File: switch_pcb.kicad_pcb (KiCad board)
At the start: 2 copper layers, 50 x 34 mm, 8 parts, among them J1 3x5mm, SW1 Microswitch

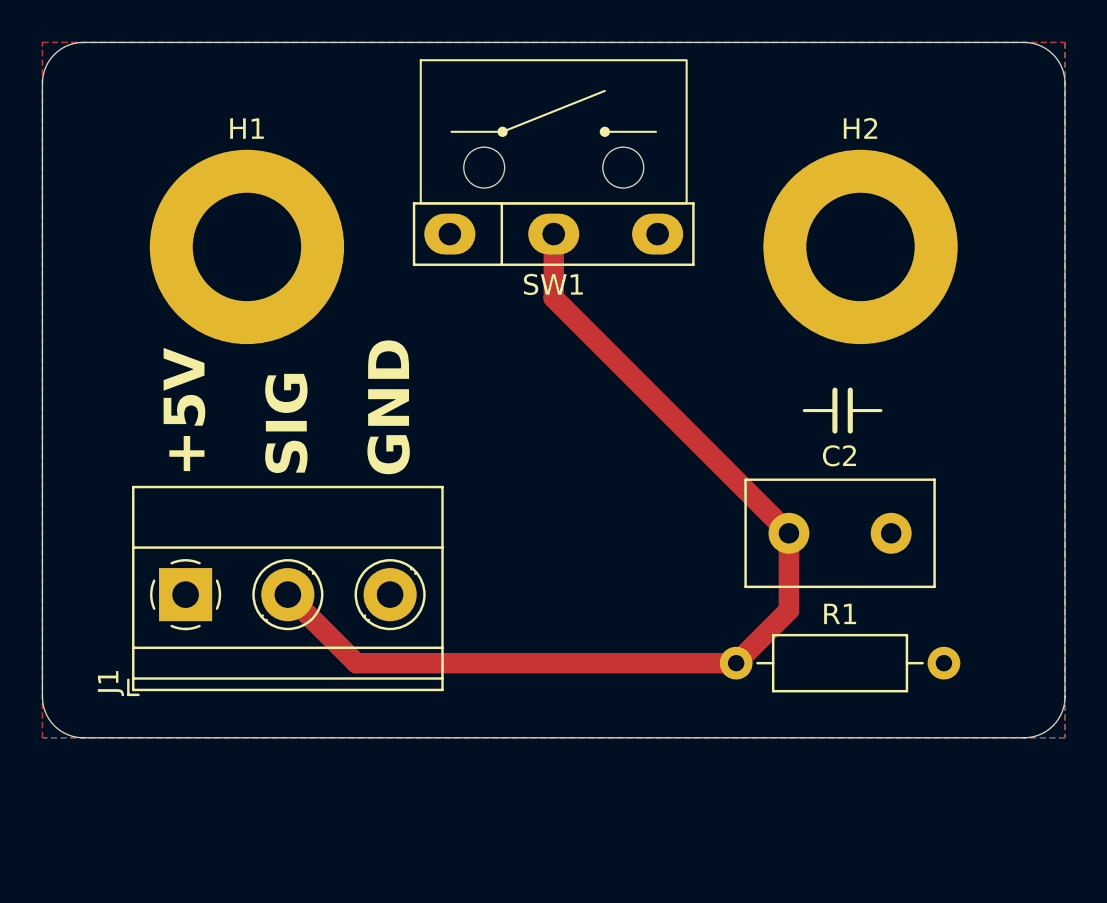
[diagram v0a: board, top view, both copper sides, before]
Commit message: Extend PCB, add course name and logo, add initial area on PCB
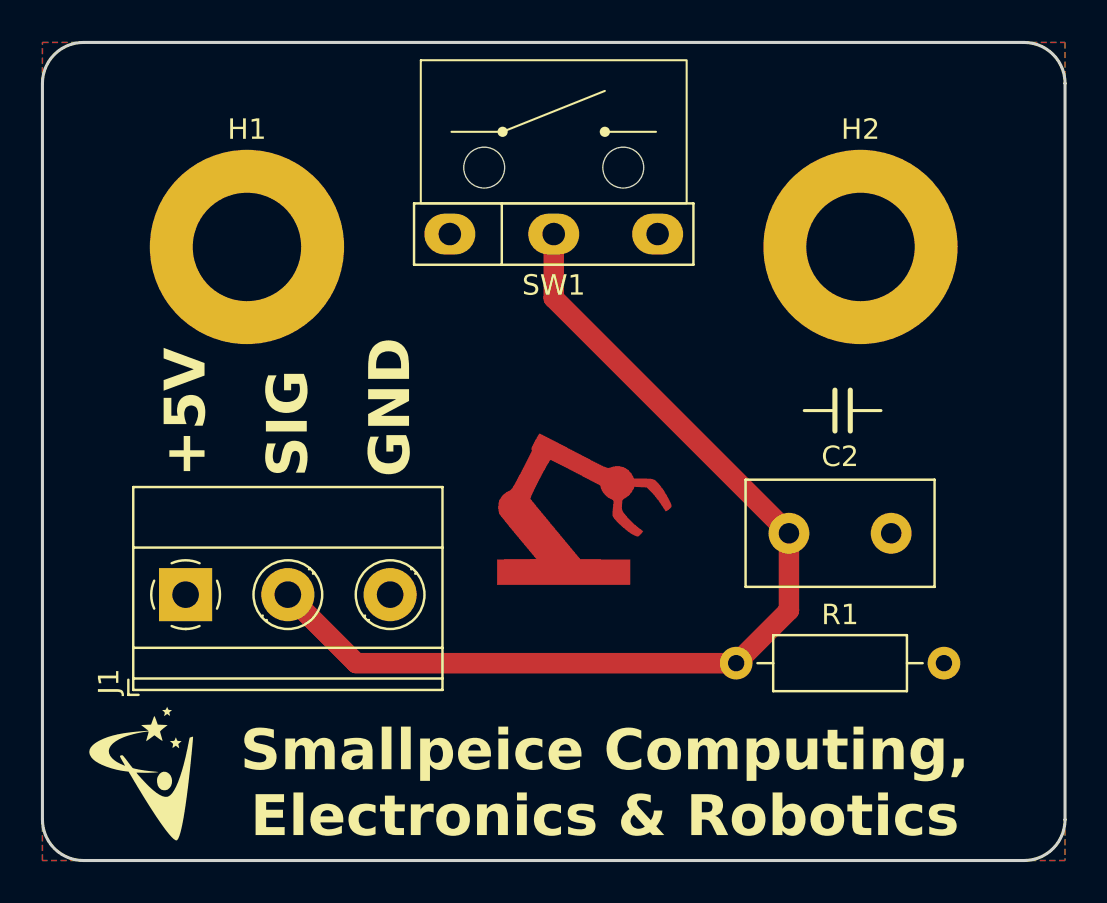
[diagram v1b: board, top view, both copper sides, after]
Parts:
- added G***: LOGO, switch_pcb:smallpeice, F.Cu at (110.8, 66.1)
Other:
- board size 50 x 34 mm -> 50 x 40 mm
- board text added: "Initials:"
- board text added: "Smallpeice Computing, Electronics & Robotics"

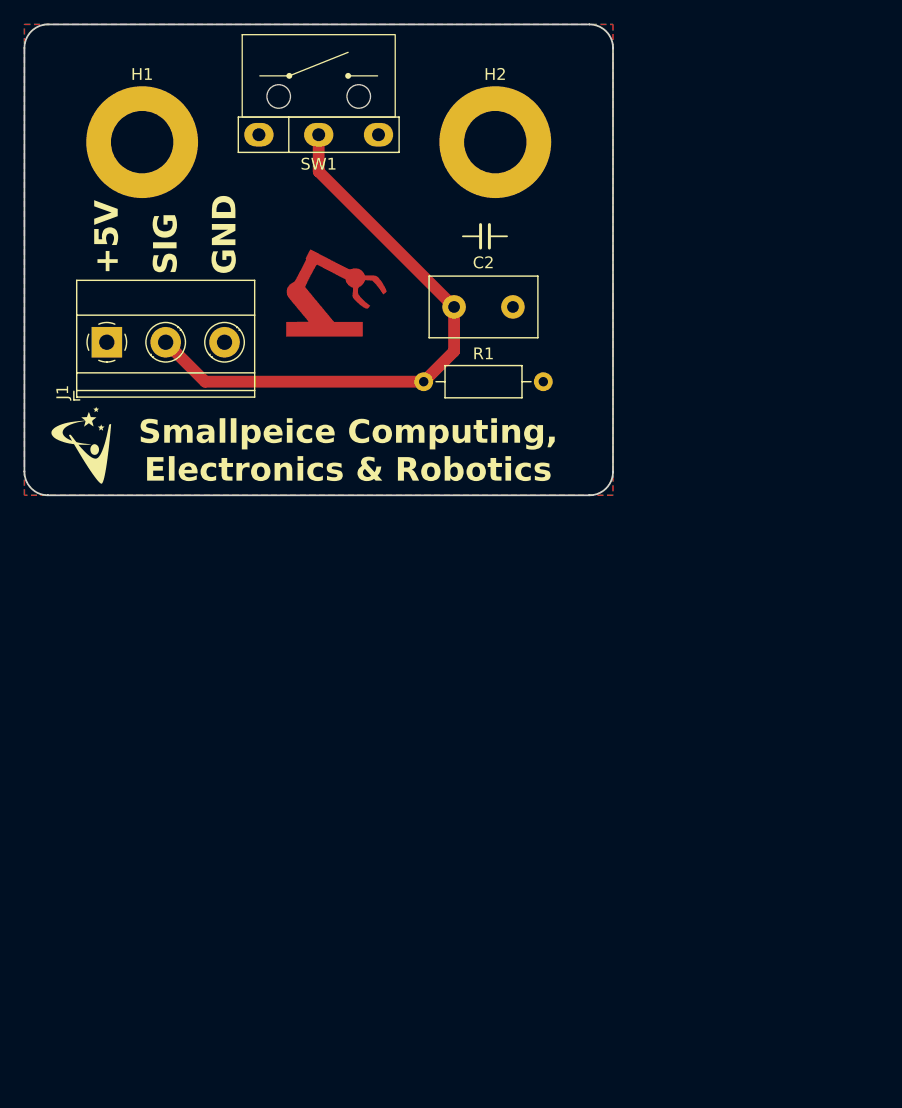
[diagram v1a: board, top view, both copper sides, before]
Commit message: Review feedback Center PCB on page Remove 5V plane & use teardrops Change circuit to be pulled up & switched low
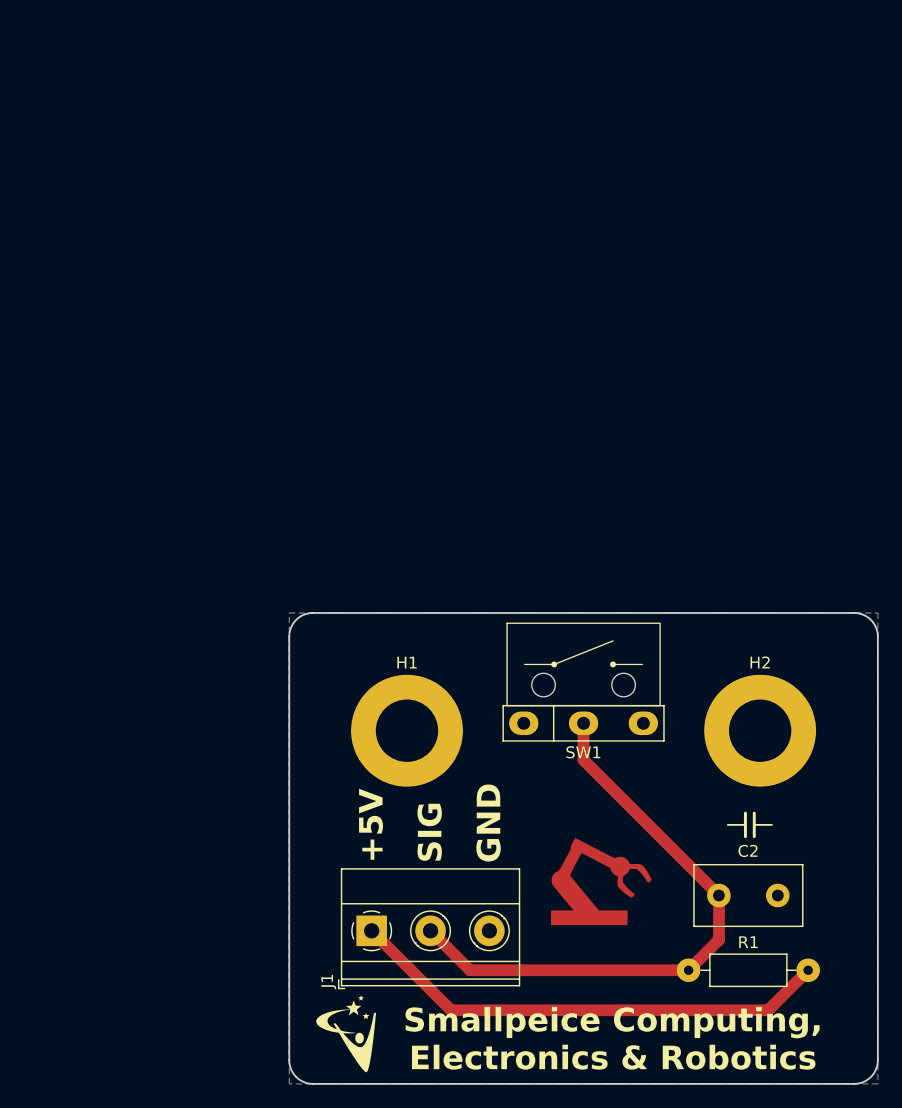
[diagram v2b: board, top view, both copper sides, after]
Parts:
- moved R1 59.7 mm to (171.6, 110.3), turned to 180 degrees
- moved C2 54.8 mm to (164.0, 104.0)
- moved G*** 54.8 mm to (133.2, 116.1)
- moved G*** 54.8 mm to (154.0, 102.8)
- moved G*** 54.8 mm to (152.8, 104.5)
- moved H1 54.8 mm to (137.5, 90.0)
- moved H2 54.8 mm to (167.5, 90.0)
- moved J1 54.8 mm to (134.5, 107.0)
- moved SW1 54.8 mm to (152.5, 89.4)
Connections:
- R1 pad 1: Net-(J1-Pin_2) -> +5V
- R1 pad 2: GND -> Net-(J1-Pin_2)
- SW1 pad 1: +5V -> GND
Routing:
- net +5V: track 0.00 -> 41.3 mm
- removed copper zone on F.Cu, net +5V
